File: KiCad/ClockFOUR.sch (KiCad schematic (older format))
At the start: 2 parts

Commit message: Schematic updated
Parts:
- added BT1: BATT_RTC, symbol BATT_RTC
- added C1, C2: 22pF, ~, symbol C
- added C3: 100nF, symbol CAP_NP
- added C32: 1000uF, 8V, TinyTiM_Lib:c_2917, symbol C_POL_1
- added C4: 100nF, ~, symbol C
- added R1: 10k, ~, symbol R
- added R2, R3: 4k7, ~, symbol R
- added R?: 500R, ~, symbol R
- added SW1: SW_RST, ~, symbol SW_PUSH
- added U1: ATMEGA328P, TQFP32, symbol ATMEGA328P
- added U2: DS3231N, symbol DS3231N
- added X1: 16MHz, ~, symbol CRYSTAL
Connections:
- net labels added: A to B, B to C, C to D, D to E, E to F, F to G, G to H, H to I, I to J, J to K, K to L, L to M, M to NC, Matrix_Pin, R to Matrix Input, SCL, SDA, VCC
- net labels removed: DI_A, DI_B, DO_A, DO_A to DI_B, DO_B to DI_C, DO_C, DO_D, DO_E, DO_M
- wire segments 62 -> 157
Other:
- note added: "14 x 13 pixel matrix"
- note removed: "The Matrix"
- moved on the sheet: L101, L102

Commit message: Schematic updated
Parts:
- added C192, C193, C33, C36: 100nF, symbol CAP_NP
- added C34, C35: 100pF, symbol CAP_NP
- added LDR1: LDR, ~, symbol VR
- added P1: ICSP, symbol CONN_6
- added P2, P3: CONN_1, symbol CONN_1
- added P4: FTDI, symbol CONN_6
- added P5: LDR_header, symbol CONN_2
- added R4: 10k, ~, symbol R
- added R5, R6: 1M, ~, symbol R
- added R8, R9: 10K, ~, symbol R
- added U31: 7805, ~, symbol 7805
- gave numbers to parts that had none: 1
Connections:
- net labels added: BUTTON_L, BUTTON_R, LDR_PIN, MATRIX_PIN, MISO, MOSI, RESET, RXD, SCK, SENSE_PIN, TXD
- net labels removed: Matrix_Pin
- wire segments 157 -> 216
- no-connect marks 3 -> 13
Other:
- note added: "Arduino"
- note added: "Cap Buttons"
- note added: "FTDI Header"
- note added: "ICSP Header"
- note added: "LDR"
- note added: "LDR Header"
- note added: "Logos"
- note added: "RTC"
- note removed: "Arduino and RTC"
- moved on the sheet: C3, C32, L101, L102, R1, R2, R3, R7, SW1, U1, U2, X1

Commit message: Schematic updated
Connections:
- wire segments 216 -> 214

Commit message: Schematic updated, board started
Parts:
- removed C1, C2: 22pF, ~, symbol C
- removed C193: 100nF, symbol CAP_NP
- removed C4: 100nF, ~, symbol C
- removed R3: 4k7, ~, symbol R
- removed U1: ATMEGA328P, TQFP32, symbol ATMEGA328P
- removed U2: DS3231N, symbol DS3231N
- removed U31: 7805, ~, symbol 7805
- added C1: 100n, symbol CAP_NP
- added C4, C6: 22p, symbol CAP_NP
- added IC1: ATMEGA328P, TQFP32, symbol ATMEGA328P
- added R9: 4K7, ~, symbol R
- added S1, S2, S3, S4: CONN_1, symbol CONN_1
- added U1: DS3231N, ~, symbol DS3231N
- C10: renamed from C192; value 100nF -> 100n
- C2: renamed from C34; value 100pF -> 100p
- C3: renamed from C35; value 100pF -> 100p
- C5: renamed from C36; value 100nF -> 100n
- C7: renamed from C33; value 100nF -> 100n
- C8: renamed from C3; value 100nF -> 100n
- C9: renamed from C32; value 1000uF, 8V -> 1000u
- R2: renamed from R1; value 10k -> 10K
- R5: renamed from R4; value 10k -> 10K
- R8: renamed from R2; value 4k7 -> 4K7
- renumbered L101 to L1, L102 to L2, P2 to P1, P3 to P2, P1 to P3, R7 to R1, R5 to R3, R6 to R4, R8 to R6, R9 to R7
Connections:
- wire segments 214 -> 213
- no-connect marks 13 -> 14
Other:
- note added: "Mounting Screws"

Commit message: Board layout updated
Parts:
- removed IC1: ATMEGA328P, TQFP32, symbol ATMEGA328P
- added P6: BARREL_JACK, symbol BARREL_JACK
- added U1: ATMEGA328P, TQFP32, symbol ATMEGA328P
- BT1: footprint (none) -> ~
- C9: value 1000u -> 47u
- renumbered U1 to U2
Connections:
- wire segments 213 -> 218
- no-connect marks 14 -> 18
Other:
- moved on the sheet: C10, C9
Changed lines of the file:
@@
 Sheet 1 14
 Title "ClockFOUR"
-Date "1 oct 2014"
+Date "2 oct 2014"
 Rev ""
 Comp "WyoLum"
@@
 C1 ED 35 72 E0 F7 FB FF F1 1F FF F1 9F FF F9 9F C7 C7 C7 73 1A 9F 2B 70 38 1C FB F6 ED 3B 79 F2
 E4 23 8F 3C 52 B0 F1 D9 2E 76 F1 FF 03 17 ED 19 47 28 92 59 FB 00 00 00 00 49 45 4E 44 AE 42 60
-82 06 $EndBitmap
+82 00 $EndBitmap
 EndData
 $EndBitmap
@@
 	0    -1   -1   0
 $EndComp
-Text GLabel 4525 7050 0    60   Input ~ 0
+Text GLabel 4825 7050 0    60   Input ~ 0
 GND
-Text GLabel 4525 6500 0    60   Input ~ 0
+Text GLabel 4825 6350 0    60   Input ~ 0
 5V
 $Sheet
@@
 L GND #PWR01
 U 1 1 50E7FAEA
-P 4700 7125
-F 0 "#PWR01" H 4700 7125 30  0001 C CNN
-F 1 "GND" H 4700 7055 30  0001 C CNN
-F 2 "" H 4700 7125 60  0001 C CNN
-F 3 "" H 4700 7125 60  0001 C CNN
-	1    4700 7125
+P 5350 7125
+F 0 "#PWR01" H 5350 7125 30  0001 C CNN
+F 1 "GND" H 5350 7055 30  0001 C CNN
+F 2 "" H 5350 7125 60  0001 C CNN
+F 3 "" H 5350 7125 60  0001 C CNN
+	1    5350 7125
 	1    0    0    -1
 $EndComp
@@
 $EndComp
 $Comp
-L BATT_RTC BT1
-U 1 1 542B38DC
-P 950 6325
-F 0 "BT1" H 1150 6450 50  0000 C CNN
-F 1 "BATT_RTC" H 800 6450 50  0000 C CNN
-F 2 "" H 950 6325 60  0000 C CNN
-F 3 "" H 950 6325 60  0000 C CNN
-F 4 "BU2032SM-HD-GCT-ND " H 1050 6625 60  0001 C CNN "Digikey"
-	1    950  6325
-	0    -1   1    0
-$EndComp
-$Comp
 L CAP_NP C8
 U 1 1 542B4ECC
@@
 L C_POL_1 C9
 U 1 1 542D4A8B
-P 5075 6750
-F 0 "C9" H 5075 6850 50  0000 L CNN
-F 1 "1000u" H 4925 6650 50  0000 L CNN
-F 2 "TinyTiM_Lib:c_2917" H 5075 6700 50  0001 C CNN
-F 3 "" H 5075 6750 60  0001 C CNN
-F 4 "CAP ALUM 47UF 8V 20% SMD" H 5075 6950 60  0001 L CNN "Field4"
-F 5 "47u,8V" H 5075 7050 60  0001 L CNN "Field5"
-F 6 "2917 (7343 Metric)" H 5075 7150 60  0001 L CNN "Field6"
-F 7 "Panasonic Electronic Components" H 5075 7250 60  0001 L CNN "Field7"
-F 8 "EEF-CD0K470R" H 5075 7350 60  0001 L CNN "Field8"
-F 9 "Digikey" H 5075 7450 60  0001 L CNN "Field9"
-F 10 "PCE3606CT-ND" H 5075 7550 60  0001 L CNN "Field10"
-F 11 "http://www.digikey.com/product-detail/en/EEF-CD0K470R/PCE3606CT-ND/614442" H 5075 7650 60  0001 L CNN "Field11"
-	1    5075 6750
+P 5725 6750
+F 0 "C9" H 5725 6850 50  0000 L CNN
+F 1 "47u" H 5575 6650 50  0000 L CNN
+F 2 "TinyTiM_Lib:c_2917" H 5725 6700 50  0001 C CNN
+F 3 "" H 5725 6750 60  0001 C CNN
+F 4 "CAP ALUM 47UF 8V 20% SMD" H 5725 6950 60  0001 L CNN "Field4"
+F 5 "47u,8V" H 5725 7050 60  0001 L CNN "Field5"
+F 6 "2917 (7343 Metric)" H 5725 7150 60  0001 L CNN "Field6"
+F 7 "Panasonic Electronic Components" H 5725 7250 60  0001 L CNN "Field7"
+F 8 "EEF-CD0K470R" H 5725 7350 60  0001 L CNN "Field8"
+F 9 "Digikey" H 5725 7450 60  0001 L CNN "Field9"
+F 10 "PCE3606CT-ND" H 5725 7550 60  0001 L CNN "Field10"
+F 11 "http://www.digikey.com/product-detail/en/EEF-CD0K470R/PCE3606CT-ND/614442" H 5725 7650 60  0001 L CNN "Field11"
+	1    5725 6750
 	1    0    0    -1
 $EndComp
@@
 L CAP_NP C10
 U 1 1 542C2DFC
-P 5425 6775
-F 0 "C10" V 5475 6925 39  0000 C CNN
-F 1 "100n" V 5475 6650 39  0000 C CNN
-F 2 "" H 5425 6775 60  0000 C CNN
-F 3 "" H 5425 6775 60  0000 C CNN
-	1    5425 6775
+P 6075 6775
+F 0 "C10" V 6125 6925 39  0000 C CNN
+F 1 "100n" V 6125 6650 39  0000 C CNN
+F 2 "" H 6075 6775 60  0000 C CNN
+F 3 "" H 6075 6775 60  0000 C CNN
+	1    6075 6775
 	1    0    0    -1
 $EndComp
@@
 $EndComp
 $Comp
-L ATMEGA328P IC1
-U 1 1 542B71EC
-P 2800 2675
-F 0 "IC1" H 2050 3925 40  0000 L BNN
-F 1 "ATMEGA328P" H 3200 1275 40  0000 L BNN
-F 2 "TQFP32" H 2800 2675 30  0000 C CIN
-F 3 "~" H 2800 2675 60  0000 C CNN
-	1    2800 2675
-	1    0    0    -1
-$EndComp
-$Comp
-L DS3231N U1
+L DS3231N U2
 U 1 1 542B8235
 P 2625 6325
-F 0 "U1" H 2925 6875 60  0000 C CNN
+F 0 "U2" H 2925 6875 60  0000 C CNN
 F 1 "DS3231N" H 2325 5925 60  0000 C CNN
 F 2 "~" H 2625 6325 60  0000 C CNN
@@
 Wire Notes Line
 	3900 7725 3900 4475
-Connection ~ 5425 7050
-Wire Wire Line
-	5425 7050 5425 6850
-Connection ~ 5300 6500
-Wire Wire Line
-	5425 6500 5425 6675
+Connection ~ 6075 7050
+Wire Wire Line
+	6075 7050 6075 6850
+Connection ~ 5950 6500
+Wire Wire Line
+	6075 6500 6075 6675
 Wire Notes Line
 	4875 4475 4875 3850
@@
 Wire Wire Line
 	5175 1250 5175 1300
-Connection ~ 5075 7050
-Wire Wire Line
-	5075 7050 5075 7000
-Connection ~ 5075 6500
-Wire Wire Line
-	5075 6500 5075 6550
+Connection ~ 5725 7050
+Wire Wire Line
+	5725 7050 5725 7000
+Connection ~ 5725 6500
+Wire Wire Line
+	5725 6500 5725 6550
 Wire Notes Line
 	11150 5950 11150 5750
@@
 Connection ~ 950  5975
 Wire Wire Line
-	1125 5975 950  5975
-Wire Wire Line
-	1125 6225 1125 5975
+	950  5975 1125 5975
+Wire Wire Line
+	1125 5975 1125 6225
 Wire Wire Line
 	950  7225 950  6525
@@
 Connection ~ 3575 6575
 Wire Wire Line
-	3525 6575 3575 6575
+	3575 6575 3525 6575
 Connection ~ 3575 6675
 Wire Wire Line
-	3525 6675 3575 6675
+	3575 6675 3525 6675
 Connection ~ 3575 6775
 Wire Wire Line
-	3525 6775 3575 6775
+	3575 6775 3525 6775
 Wire Wire Line
 	3575 6375 3575 7225
@@
 L PWR_FLAG #FLG011
 U 1 1 542C2187
-P 4700 6500
-F 0 "#FLG011" H 4700 6595 30  0001 C CNN
-F 1 "PWR_FLAG" H 4700 6680 30  0000 C CNN
-F 2 "" H 4700 6500 60  0000 C CNN
-F 3 "" H 4700 6500 60  0000 C CNN
-	1    4700 6500
-	1    0    0    -1
-$EndComp
-Connection ~ 4700 6500
+P 5100 6350
+F 0 "#FLG011" H 5100 6445 30  0001 C CNN
+F 1 "PWR_FLAG" H 5100 6530 30  0000 C CNN
+F 2 "" H 5100 6350 60  0000 C CNN
+F 3 "" H 5100 6350 60  0000 C CNN
+	1    5100 6350
+	1    0    0    -1
+$EndComp
 $Comp
 L PWR_FLAG #FLG012
 U 1 1 542C219E
-P 4700 7050
-F 0 "#FLG012" H 4700 7145 30  0001 C CNN
-F 1 "PWR_FLAG" H 4700 7230 30  0000 C CNN
-F 2 "" H 4700 7050 60  0000 C CNN
-F 3 "" H 4700 7050 60  0000 C CNN
-	1    4700 7050
-	1    0    0    -1
-$EndComp
-Connection ~ 4700 7050
+P 5350 7050
+F 0 "#FLG012" H 5350 7145 30  0001 C CNN
+F 1 "PWR_FLAG" H 5350 7230 30  0000 C CNN
+F 2 "" H 5350 7050 60  0000 C CNN
+F 3 "" H 5350 7050 60  0000 C CNN
+	1    5350 7050
+	1    0    0    -1
+$EndComp
+Connection ~ 5350 7050
 $Comp
 L CAP_NP C4
@@
 	1    0    0    -1
 $EndComp
-Connection ~ 5425 6500
-Wire Wire Line
-	4700 7125 4700 7050
-Wire Wire Line
-	4525 7050 5425 7050
-Wire Wire Line
-	4525 6500 5575 6500
+Connection ~ 6075 6500
+Wire Wire Line
+	5350 7050 5350 7125
+Wire Wire Line
+	4825 7050 6075 7050
+Wire Wire Line
+	4950 6500 6225 6500
 $Comp
 L VCC #PWR013
 U 1 1 542BE803
-P 5575 6500
-F 0 "#PWR013" H 5575 6600 30  0001 C CNN
-F 1 "VCC" H 5575 6600 30  0000 C CNN
-F 2 "" H 5575 6500 60  0000 C CNN
-F 3 "" H 5575 6500 60  0000 C CNN
-	1    5575 6500
+P 6225 6500
+F 0 "#PWR013" H 6225 6600 30  0001 C CNN
+F 1 "VCC" H 6225 6600 30  0000 C CNN
+F 2 "" H 6225 6500 60  0000 C CNN
+F 3 "" H 6225 6500 60  0000 C CNN
+	1    6225 6500
 	1    0    0    -1
 $EndComp
@@
 	1    0    0    -1
 $EndComp
+NoConn ~ 6300 4575
+NoConn ~ 6300 4675
+NoConn ~ 5900 4675
+NoConn ~ 5900 4575
+$Comp
+L BATT_RTC BT1
+U 1 1 542CF9F1
+P 950 6325
+F 0 "BT1" H 900 6125 50  0000 C CNN
+F 1 "BATT_RTC" H 900 6200 50  0000 C CNN
+F 2 "~" H 950 6325 60  0000 C CNN
+F 3 "~" H 950 6325 60  0000 C CNN
+F 4 "BU2032SM-HD-GCT-ND " H 1050 6625 60  0001 C CNN "Digikey"
+	1    950  6325
+	0    1    1    0
+$EndComp
+$Comp
+L ATMEGA328P U1
+U 1 1 542D5902
+P 2750 2250
+F 0 "U1" H 2000 3500 40  0000 L BNN
+F 1 "ATMEGA328P" H 3150 850 40  0000 L BNN
+F 2 "TQFP32" H 2750 2250 30  0000 C CIN
+F 3 "~" H 2750 2250 60  0000 C CNN
+	1    2750 2250
+	1    0    0    -1
+$EndComp
+$Comp
+L BARREL_JACK P6
+U 1 1 542DBC93
+P 4650 6600
+F 0 "P6" H 4325 6425 60  0000 C CNN
+F 1 "BARREL_JACK" H 4725 6425 60  0000 C CNN
+F 2 "" H 4650 6600 60  0000 C CNN
+F 3 "" H 4650 6600 60  0000 C CNN
+	1    4650 6600
+	1    0    0    -1
+$EndComp
+Wire Wire Line
+	4950 6600 5100 6600
+Wire Wire Line
+	5100 6600 5100 7050
+Wire Wire Line
+	4950 6700 5100 6700
+Connection ~ 5100 6700
+Connection ~ 5100 7050
+Wire Wire Line
+	4825 6350 5100 6350
+Wire Wire Line
+	5100 6350 5100 6500
+Connection ~ 5100 6500
 $EndSCHEMATC

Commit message: Board layout updated
Matrix placed and wired. Added RTC.
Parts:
- added C3: 100n, symbol CAP_NP
- renumbered C9 to C10, C10 to C11, C3 to C4, C4 to C5, C5 to C6, C6 to C7, C7 to C8, C8 to C9
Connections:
- wire segments 218 -> 220
- no-connect marks 18 -> 17
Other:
- moved on the sheet: U1

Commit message: Layout updated
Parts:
- removed P1, P2: CONN_1, symbol CONN_1
- added P4: Button_Header, symbol CONN_2
- X1: value 16MHz -> CRYSTAL
- renumbered P3 to P1, P4 to P2, P5 to P3, P6 to P5
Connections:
- wire segments 220 -> 222
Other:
- note added: "Touch Header"

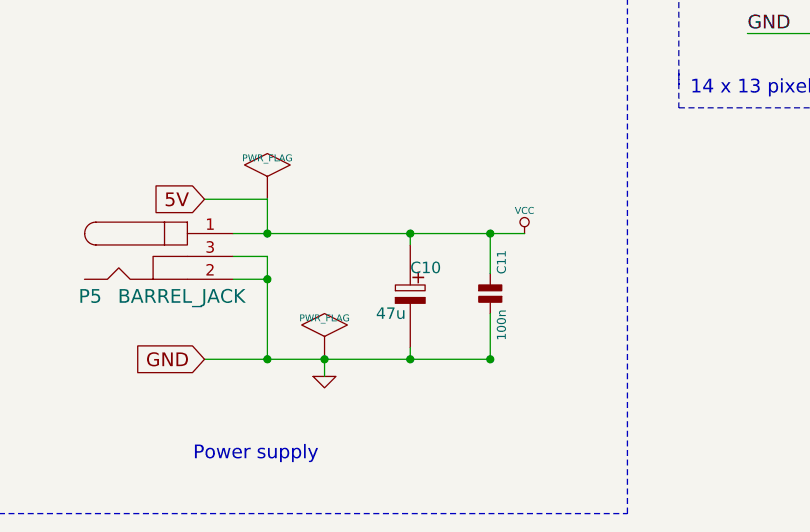
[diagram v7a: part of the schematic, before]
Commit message: Layout updated
added 4x caps on power input.  Replace with single larger cap??
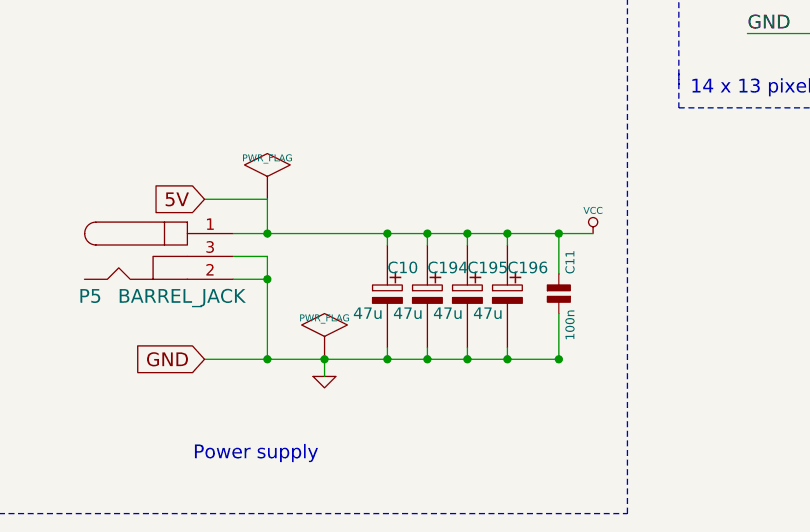
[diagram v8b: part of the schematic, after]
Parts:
- added C194, C195, C196: 47u, TinyTiM_Lib:c_2917, symbol C_POL_1
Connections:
- wire segments 222 -> 228
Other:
- moved on the sheet: C10, C11
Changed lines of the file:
@@
 C1 ED 35 72 E0 F7 FB FF F1 1F FF F1 9F FF F9 9F C7 C7 C7 73 1A 9F 2B 70 38 1C FB F6 ED 3B 79 F2
 E4 23 8F 3C 52 B0 F1 D9 2E 76 F1 FF 03 17 ED 19 47 28 92 59 FB 00 00 00 00 49 45 4E 44 AE 42 60
-82 08 $EndBitmap
+82 00 $EndBitmap
 EndData
 $EndBitmap
@@
 L C_POL_1 C10
 U 1 1 542D4A8B
-P 5725 6750
-F 0 "C10" H 5725 6850 50  0000 L CNN
-F 1 "47u" H 5575 6650 50  0000 L CNN
-F 2 "TinyTiM_Lib:c_2917" H 5725 6700 50  0001 C CNN
-F 3 "" H 5725 6750 60  0001 C CNN
-F 4 "CAP ALUM 47UF 8V 20% SMD" H 5725 6950 60  0001 L CNN "Field4"
-F 5 "47u,8V" H 5725 7050 60  0001 L CNN "Field5"
-F 6 "2917 (7343 Metric)" H 5725 7150 60  0001 L CNN "Field6"
-F 7 "Panasonic Electronic Components" H 5725 7250 60  0001 L CNN "Field7"
-F 8 "EEF-CD0K470R" H 5725 7350 60  0001 L CNN "Field8"
-F 9 "Digikey" H 5725 7450 60  0001 L CNN "Field9"
-F 10 "PCE3606CT-ND" H 5725 7550 60  0001 L CNN "Field10"
-F 11 "http://www.digikey.com/product-detail/en/EEF-CD0K470R/PCE3606CT-ND/614442" H 5725 7650 60  0001 L CNN "Field11"
-	1    5725 6750
+P 5625 6750
+F 0 "C10" H 5625 6850 50  0000 L CNN
+F 1 "47u" H 5475 6650 50  0000 L CNN
+F 2 "TinyTiM_Lib:c_2917" H 5625 6700 50  0001 C CNN
+F 3 "" H 5625 6750 60  0001 C CNN
+F 4 "CAP ALUM 47UF 8V 20% SMD" H 5625 6950 60  0001 L CNN "Field4"
+F 5 "47u,8V" H 5625 7050 60  0001 L CNN "Field5"
+F 6 "2917 (7343 Metric)" H 5625 7150 60  0001 L CNN "Field6"
+F 7 "Panasonic Electronic Components" H 5625 7250 60  0001 L CNN "Field7"
+F 8 "EEF-CD0K470R" H 5625 7350 60  0001 L CNN "Field8"
+F 9 "Digikey" H 5625 7450 60  0001 L CNN "Field9"
+F 10 "PCE3606CT-ND" H 5625 7550 60  0001 L CNN "Field10"
+F 11 "http://www.digikey.com/product-detail/en/EEF-CD0K470R/PCE3606CT-ND/614442" H 5625 7650 60  0001 L CNN "Field11"
+	1    5625 6750
 	1    0    0    -1
 $EndComp
@@
 L CAP_NP C11
 U 1 1 542C2DFC
-P 6075 6775
-F 0 "C11" V 6125 6925 39  0000 C CNN
-F 1 "100n" V 6125 6650 39  0000 C CNN
-F 2 "" H 6075 6775 60  0000 C CNN
-F 3 "" H 6075 6775 60  0000 C CNN
-	1    6075 6775
+P 6375 6775
+F 0 "C11" V 6425 6925 39  0000 C CNN
+F 1 "100n" V 6425 6650 39  0000 C CNN
+F 2 "" H 6375 6775 60  0000 C CNN
+F 3 "" H 6375 6775 60  0000 C CNN
+	1    6375 6775
 	1    0    0    -1
 $EndComp
@@
 L VCC #PWR8
 U 1 1 542BE803
-P 6225 6500
-F 0 "#PWR8" H 6225 6600 30  0001 C CNN
-F 1 "VCC" H 6225 6600 30  0000 C CNN
-F 2 "" H 6225 6500 60  0000 C CNN
-F 3 "" H 6225 6500 60  0000 C CNN
-	1    6225 6500
+P 6525 6500
+F 0 "#PWR8" H 6525 6600 30  0001 C CNN
+F 1 "VCC" H 6525 6600 30  0000 C CNN
+F 2 "" H 6525 6500 60  0000 C CNN
+F 3 "" H 6525 6500 60  0000 C CNN
+	1    6525 6500
 	1    0    0    -1
 $EndComp
@@
 	4875 5000 6675 5000
 Wire Wire Line
-	4950 6500 6225 6500
-Wire Wire Line
-	4825 7050 6075 7050
+	4950 6500 6525 6500
+Wire Wire Line
+	4825 7050 6375 7050
 Wire Wire Line
 	5350 7050 5350 7125
-Connection ~ 6075 6500
+Connection ~ 6375 6500
 Wire Wire Line
 	1125 3450 1125 3350
@@
 	11150 5950 11150 5750
 Wire Wire Line
-	5725 6500 5725 6550
-Connection ~ 5725 6500
-Wire Wire Line
-	5725 7050 5725 7000
-Connection ~ 5725 7050
-Wire Wire Line
 	5175 1250 5175 1300
 Wire Wire Line
@@
 	4875 3850 4875 5000
 Wire Wire Line
-	6075 6500 6075 6675
-Wire Wire Line
-	6075 7050 6075 6850
-Connection ~ 6075 7050
+	6375 6500 6375 6675
+Wire Wire Line
+	6375 7050 6375 6850
+Connection ~ 6375 7050
 Wire Notes Line
 	3900 7725 3900 4475
@@
 Wire Wire Line
 	3750 6275 3525 6275
+$Comp
+L C_POL_1 C194
+U 1 1 54323DA9
+P 5800 6750
+F 0 "C194" H 5800 6850 50  0000 L CNN
+F 1 "47u" H 5650 6650 50  0000 L CNN
+F 2 "TinyTiM_Lib:c_2917" H 5800 6700 50  0001 C CNN
+F 3 "" H 5800 6750 60  0001 C CNN
+F 4 "CAP ALUM 47UF 8V 20% SMD" H 5800 6950 60  0001 L CNN "Field4"
+F 5 "47u,8V" H 5800 7050 60  0001 L CNN "Field5"
+F 6 "2917 (7343 Metric)" H 5800 7150 60  0001 L CNN "Field6"
+F 7 "Panasonic Electronic Components" H 5800 7250 60  0001 L CNN "Field7"
+F 8 "EEF-CD0K470R" H 5800 7350 60  0001 L CNN "Field8"
+F 9 "Digikey" H 5800 7450 60  0001 L CNN "Field9"
+F 10 "PCE3606CT-ND" H 5800 7550 60  0001 L CNN "Field10"
+F 11 "http://www.digikey.com/product-detail/en/EEF-CD0K470R/PCE3606CT-ND/614442" H 5800 7650 60  0001 L CNN "Field11"
+	1    5800 6750
+	1    0    0    -1
+$EndComp
+$Comp
+L C_POL_1 C195
+U 1 1 54323DB7
+P 5975 6750
+F 0 "C195" H 5975 6850 50  0000 L CNN
+F 1 "47u" H 5825 6650 50  0000 L CNN
+F 2 "TinyTiM_Lib:c_2917" H 5975 6700 50  0001 C CNN
+F 3 "" H 5975 6750 60  0001 C CNN
+F 4 "CAP ALUM 47UF 8V 20% SMD" H 5975 6950 60  0001 L CNN "Field4"
+F 5 "47u,8V" H 5975 7050 60  0001 L CNN "Field5"
+F 6 "2917 (7343 Metric)" H 5975 7150 60  0001 L CNN "Field6"
+F 7 "Panasonic Electronic Components" H 5975 7250 60  0001 L CNN "Field7"
+F 8 "EEF-CD0K470R" H 5975 7350 60  0001 L CNN "Field8"
+F 9 "Digikey" H 5975 7450 60  0001 L CNN "Field9"
+F 10 "PCE3606CT-ND" H 5975 7550 60  0001 L CNN "Field10"
+F 11 "http://www.digikey.com/product-detail/en/EEF-CD0K470R/PCE3606CT-ND/614442" H 5975 7650 60  0001 L CNN "Field11"
+	1    5975 6750
+	1    0    0    -1
+$EndComp
+$Comp
+L C_POL_1 C196
+U 1 1 54323DC5
+P 6150 6750
+F 0 "C196" H 6150 6850 50  0000 L CNN
+F 1 "47u" H 6000 6650 50  0000 L CNN
+F 2 "TinyTiM_Lib:c_2917" H 6150 6700 50  0001 C CNN
+F 3 "" H 6150 6750 60  0001 C CNN
+F 4 "CAP ALUM 47UF 8V 20% SMD" H 6150 6950 60  0001 L CNN "Field4"
+F 5 "47u,8V" H 6150 7050 60  0001 L CNN "Field5"
+F 6 "2917 (7343 Metric)" H 6150 7150 60  0001 L CNN "Field6"
+F 7 "Panasonic Electronic Components" H 6150 7250 60  0001 L CNN "Field7"
+F 8 "EEF-CD0K470R" H 6150 7350 60  0001 L CNN "Field8"
+F 9 "Digikey" H 6150 7450 60  0001 L CNN "Field9"
+F 10 "PCE3606CT-ND" H 6150 7550 60  0001 L CNN "Field10"
+F 11 "http://www.digikey.com/product-detail/en/EEF-CD0K470R/PCE3606CT-ND/614442" H 6150 7650 60  0001 L CNN "Field11"
+	1    6150 6750
+	1    0    0    -1
+$EndComp
+Wire Wire Line
+	5625 6550 5625 6500
+Connection ~ 5625 6500
+Wire Wire Line
+	5800 6550 5800 6500
+Connection ~ 5800 6500
+Wire Wire Line
+	5975 6550 5975 6500
+Connection ~ 5975 6500
+Wire Wire Line
+	6150 6550 6150 6500
+Connection ~ 6150 6500
+Wire Wire Line
+	5625 7000 5625 7050
+Connection ~ 5625 7050
+Wire Wire Line
+	5800 7000 5800 7050
+Connection ~ 5800 7050
+Wire Wire Line
+	5975 7000 5975 7050
+Connection ~ 5975 7050
+Wire Wire Line
+	6150 7000 6150 7050
+Connection ~ 6150 7050
 $EndSCHEMATC
